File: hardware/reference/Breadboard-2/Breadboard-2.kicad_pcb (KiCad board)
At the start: 2 copper layers, 50.8 x 76.2 mm, 75 parts, among them J1 01x06, J2 01x06, J3 01x05, J4 01x07, J5 01x05S, Q31 BSS138K, Q51 SSM3J356R,LF, Q52 SSM3J356R,LF, Q53 DTC143ZCA, Q54 DTC143ZCA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

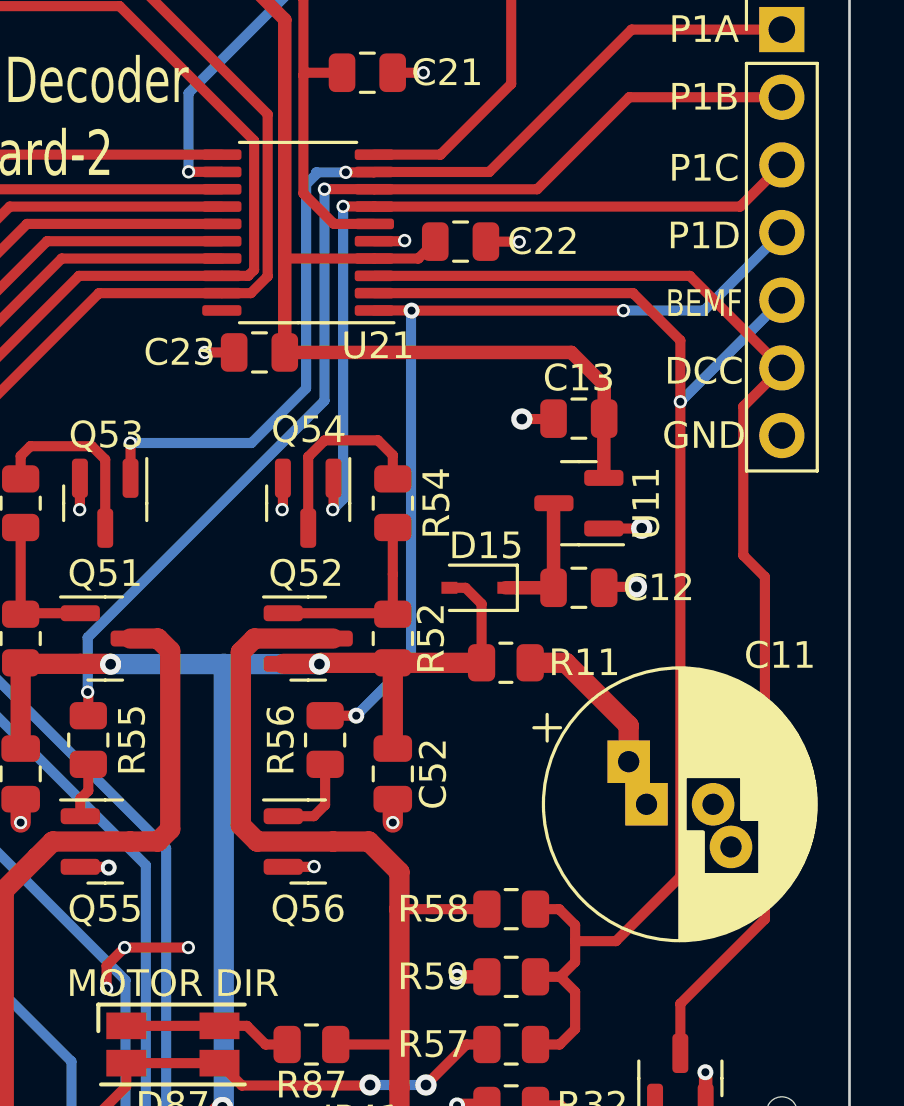
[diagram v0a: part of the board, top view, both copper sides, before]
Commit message: Move DCC_IN and BackEMF to pins with appropriate capabilities.
STM32 does not allow software remapping of the periperhal input
pins.  The location in the PIC design (Breadboard-1) routes them
to pins on an STM32 that are designed for the oscellator, but can
be re-used.  As such they have no ADC or Timer triggers attached
to them.

DCC_IN was moved to port 20, which can be routed to any of
TIM1_CH2, TIM2_CH2, TIM3_CH1, TIM3_CH2, TIM1_CH3, TIM16_CH1N.

BackEMF was moved to pin 7, which can be routed to ADC_IN0.

The displaced P1C H-Bridge output was moved to pin 2, as it's more
than capable of outputting the necessary signal.
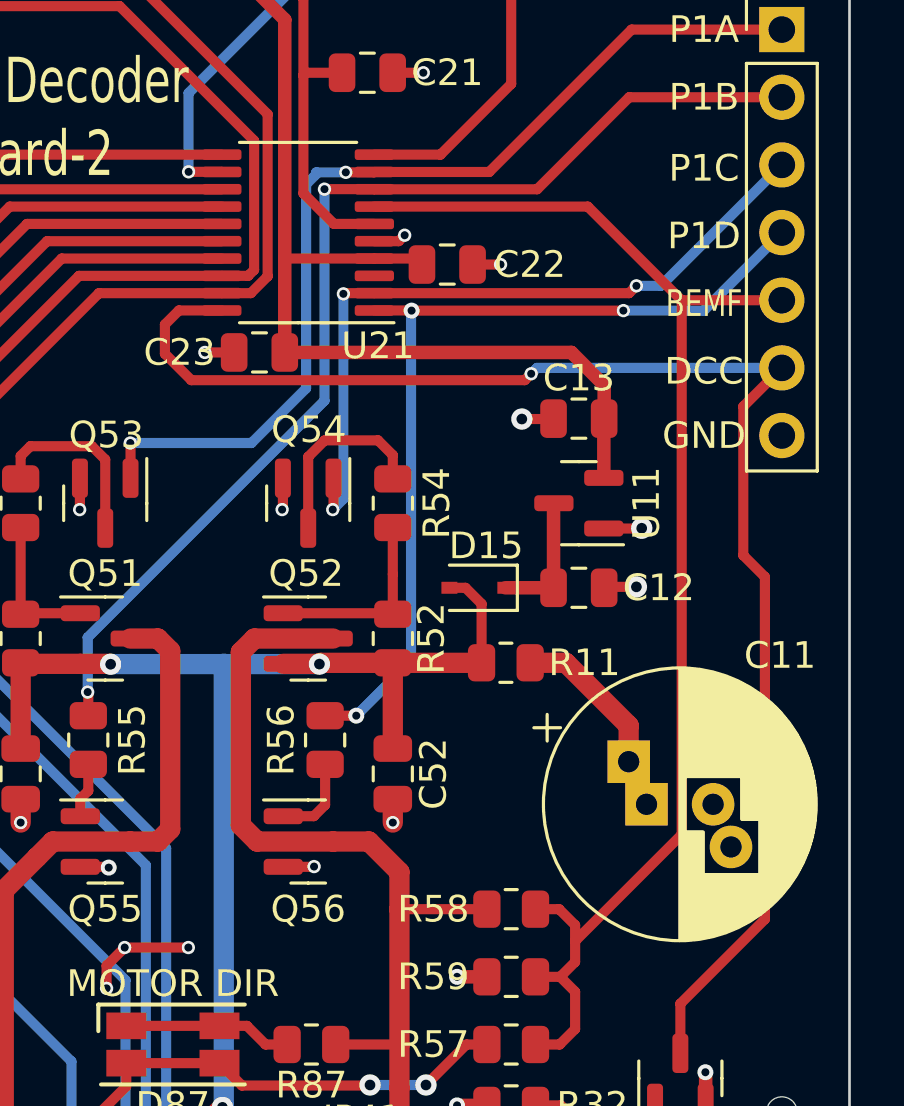
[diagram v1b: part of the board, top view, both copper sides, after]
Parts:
- moved C22 0.99 mm to (86.5, 64.7)
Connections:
- U21 pad 2: BackEMF -> P1C
- U21 pad 20: unconnected-(U21-Pad20) -> DCC_IN
- U21 pad 3: DCC_IN -> unconnected-(U21-Pad3)
- U21 pad 7: P1C -> BackEMF
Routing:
- net DCC_IN: track 44.7 -> 55.2 mm, vias 0 -> 1
- net P1C: track 29.9 -> 27.9 mm, vias 2 -> 3
- net +3V3: track 52.9 -> 52.2 mm
- net BackEMF: track 51.4 -> 51.2 mm, vias 1 -> 0
